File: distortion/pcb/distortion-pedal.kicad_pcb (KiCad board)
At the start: 4 copper layers, 29 x 45.2 mm, 73 parts, among them J1 AudioJack2_Ground, J2 AudioJack2_Ground, J3 USB4125-GF-A-0190, J4 Barrel_Jack, SW1 SW_DPDT_x2, U1 LMR62014XMF-NOPB, U2 TL081H, U3 TL081H, U4 TL081H, U5 TLV767, U6 TL081H

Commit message: distortion rev 3
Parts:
- removed RD3: R, Resistor_SMD:R_0805_2012Metric_Pad1.20x1.40mm_HandSolder
- added R18: R, Resistor_SMD:R_0805_2012Metric_Pad1.20x1.40mm_HandSolder, F.Cu at (54.1, 62.3)
- added R9: R, Resistor_SMD:R_0805_2012Metric_Pad1.20x1.40mm_HandSolder, F.Cu at (51.8, 66.7)
- added RF2: R, Resistor_SMD:R_0805_2012Metric_Pad1.20x1.40mm_HandSolder, F.Cu at (49.5, 65.1)
- D6: footprint Connector_PinHeader_2.54mm:PinHeader_1x02_P2.54mm_Vertical -> effect_pedal:led_wired_1_pin
- Gain1, Level1: footprint Connector_PinHeader_2.54mm:PinHeader_1x03_P2.54mm_Vertical -> effect_pedal:potentiometer_wired_23_connected
- J1, J2: footprint Connector_PinHeader_2.54mm:PinHeader_1x02_P2.54mm_Vertical -> effect_pedal:audio_jack_wired
- J4: footprint Connector_PinHeader_2.54mm:PinHeader_1x02_P2.54mm_Vertical -> effect_pedal:barrel_jack_wired
- L1: footprint Inductor_SMD:L_Abracon_ASPI-3012S -> Inductor_SMD:L_0805_2012Metric_Pad1.15x1.40mm_HandSolder
- SW1: footprint Connector_PinHeader_2.54mm:PinHeader_2x03_P2.54mm_Vertical -> effect_pedal:switch_wired
- Tone1: footprint Connector_PinHeader_2.54mm:PinHeader_1x03_P2.54mm_Vertical -> effect_pedal:potentiometer_wired_12_connected
- moved RF1 11.5 mm to (47.4, 65.1), turned to 90 degrees
- moved U3 9.32 mm to (67.4, 64.2)
- moved TP6 9.21 mm to (69.4, 67.4)
- moved R13 8.79 mm to (67.4, 68.5)
- moved D6 8.62 mm to (64.8, 69.4), turned to 180 degrees
- moved C8 8.11 mm to (69.8, 70.4)
- moved R4 8.08 mm to (71.2, 64.5), turned to 90 degrees
- moved R14 8.07 mm to (59.6, 74.8), turned to 90 degrees
- moved J1 7.91 mm to (48.3, 75.2), turned to 0 degrees
- moved J2 7.90 mm to (72.5, 75.2), turned to 180 degrees
- moved C6 7.12 mm to (62.8, 64.8), turned to 180 degrees
- moved SW1 7.10 mm to (64.7, 73.7), turned to 0 degrees
- moved C10 6.79 mm to (71.2, 60.2), turned to 90 degrees
- moved H4 6.52 mm to (73.0, 71.4)
- moved H3 6.52 mm to (48.0, 71.4)
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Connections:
- JPF1 pad 1: effect_in -> Net-(JPF1-Pad1)
- RD1 pad 1: effect_in -> Net-(JPF1-Pad1)
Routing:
- net +8V: track 10.0 -> 28.7 mm
- net +5V: track 14.9 -> 30.7 mm
- net +9V: track 0.00 -> 13.8 mm
- net Net-(D2-Pad2): track 0.00 -> 11.7 mm
- net Net-(C5-Pad2): track 0.00 -> 10.1 mm
- net Net-(JPF1-Pad1): track 0.00 -> 10.00 mm
- net Net-(C8-Pad1): track 0.00 -> 8.07 mm
- net Net-(Level1-Pad1): track 0.00 -> 7.24 mm
- net +4V: track 5.40 -> 12.6 mm
- net effect_in: track 4.24 -> 11.0 mm
- net Net-(C5-Pad1): track 0.00 -> 6.57 mm
- net Net-(D5-Pad2): track 0.00 -> 6.33 mm
- net Net-(C12-Pad2): track 0.00 -> 5.70 mm
- net Net-(R6-Pad2): track 4.43 -> 10.0 mm
- net Net-(D1-Pad1): track 26.7 -> 32.0 mm
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- removed copper zone on F.Cu, net +4V
- removed copper zone on F.Cu, net +5V
- removed copper zone on F.Cu, net +8V
- removed copper zone on F.Cu, net +9V
- removed copper zone on F.Cu, net Net-(C10-Pad1)
- removed copper zone on F.Cu, net Net-(C12-Pad2)
- removed copper zone on F.Cu, net Net-(C5-Pad1)
- removed copper zone on F.Cu, net Net-(C5-Pad2)
- removed copper zone on F.Cu, net Net-(C8-Pad1)
- removed copper zone on F.Cu, net Net-(D1-Pad1)
- removed copper zone on F.Cu, net Net-(D1-Pad2)
- removed copper zone on F.Cu, net Net-(D2-Pad2)
- removed copper zone on F.Cu, net Net-(D3-Pad2)
- removed copper zone on F.Cu, net Net-(D5-Pad2)
- removed copper zone on F.Cu, net Net-(D6-Pad2)
- removed copper zone on F.Cu, net Net-(Gain1-Pad2)
- removed copper zone on F.Cu, net Net-(J2-Pad2)
- removed copper zone on F.Cu, net Net-(JP2-Pad1)
- removed copper zone on F.Cu, net Net-(JPF1-Pad2)
- removed copper zone on F.Cu, net Net-(Level1-Pad1)
- removed copper zone on F.Cu, net Net-(R4-Pad1)
- removed copper zone on F.Cu, net Net-(R6-Pad1)
- removed copper zone on F.Cu, net Net-(R6-Pad2)
- removed copper zone on F.Cu, net audio_in
- removed copper zone on F.Cu, net effect_in
- removed copper zone on F.Cu, net effect_out
- removed copper zone on F.Cu, net gain_out
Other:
- board size 29 x 45.2 mm -> 30 x 37 mm
- board text added: "Fuzz/Distortion Pedal REV3"
- board text removed: "Fuzz/Distortion Pedal REV2"

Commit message: fix project error
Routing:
- net GND: vias 20 -> 24
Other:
- board text removed: "Active"

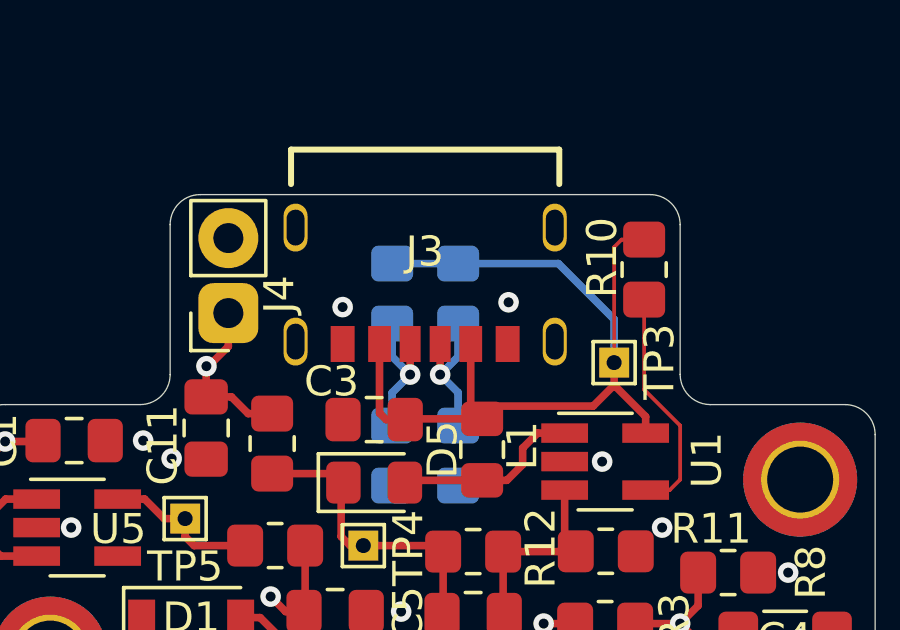
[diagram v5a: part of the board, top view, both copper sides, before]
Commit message: minor circuit rework for better use with multiple projects
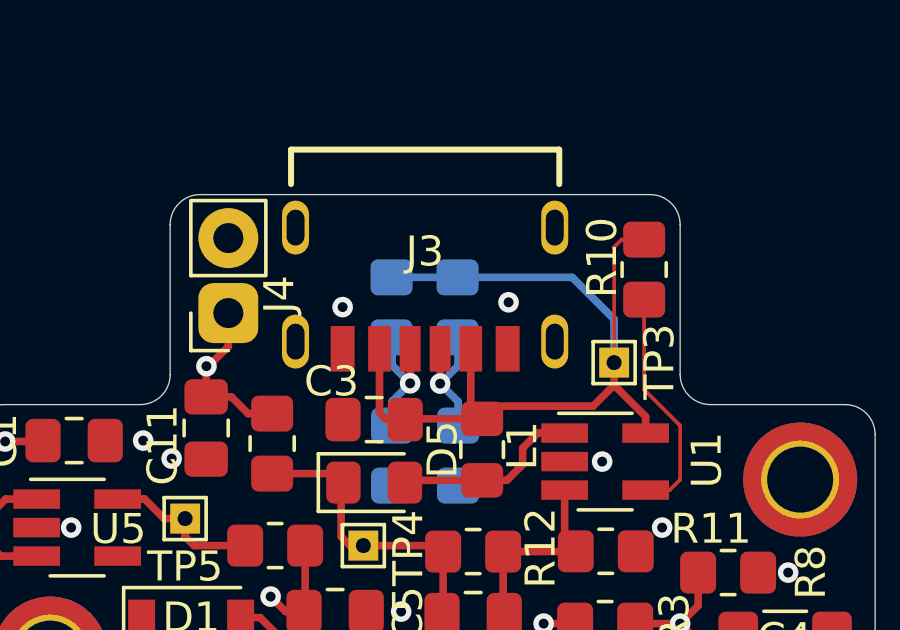
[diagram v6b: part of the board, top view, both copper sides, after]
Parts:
- moved Rcc3 0.46 mm to (61.6, 43.8)
- moved Rcc4 0.46 mm to (59.4, 43.8)
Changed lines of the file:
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@@
     (thickness 1.595)
   )
-  (paper "A4")
+  (paper "A5")
+  (title_block
+    (title "Distortion Pedal")
+  )
   (layers
     (0 "F.Cu" signal "Front")
@@
       (effects (font (size 1 1) (thickness 0.15)))
     )
-    (fp_line (start -4.47 2.25) (end -4.47 3.4) (layer "F.SilkS") (width 0.2))
     (fp_line (start -4.47 3.4) (end 4.47 3.4) (layer "F.SilkS") (width 0.2))
     (fp_line (start 4.47 3.4) (end 4.47 2.25) (layer "F.SilkS") (width 0.2))
-    (fp_line (start 5.15 3.65) (end -5.15 3.65) (layer "F.CrtYd") (width 0.05))
+    (fp_line (start -4.47 2.25) (end -4.47 3.4) (layer "F.SilkS") (width 0.2))
     (fp_line (start -5.15 -4.35) (end 5.15 -4.35) (layer "F.CrtYd") (width 0.05))
     (fp_line (start -5.15 3.65) (end -5.15 -4.35) (layer "F.CrtYd") (width 0.05))
     (fp_line (start 5.15 -4.35) (end 5.15 3.65) (layer "F.CrtYd") (width 0.05))
+    (fp_line (start 5.15 3.65) (end -5.15 3.65) (layer "F.CrtYd") (width 0.05))
+    (fp_line (start -4.47 3.4) (end -4.47 -3.4) (layer "F.Fab") (width 0.1))
     (fp_line (start 4.47 3.4) (end -4.47 3.4) (layer "F.Fab") (width 0.1))
-    (fp_line (start -4.47 3.4) (end -4.47 -3.4) (layer "F.Fab") (width 0.1))
+    (fp_line (start 4.47 -3.4) (end 4.47 3.4) (layer "F.Fab") (width 0.1))
     (fp_line (start -4.47 -3.4) (end 4.47 -3.4) (layer "F.Fab") (width 0.1))
-    (fp_line (start 4.47 -3.4) (end 4.47 3.4) (layer "F.Fab") (width 0.1))
-    (pad "A5" smd rect (at -0.5 -3.08 180) (size 0.7 1.2) (layers "F.Cu" "F.Paste" "F.Mask")
+    (pad "A5" smd rect (at -0.5 -3.24 180) (size 0.7 1.52) (layers "F.Cu" "F.Paste" "F.Mask")
       (net 16 "Net-(J3-PadA5)") (pinfunction "CC1") (pintype "bidirectional"))
-    (pad "A9" smd rect (at 1.52 -3.08 180) (size 0.76 1.2) (layers "F.Cu" "F.Paste" "F.Mask")
+    (pad "A9" smd rect (at 1.52 -3.24 180) (size 0.76 1.52) (layers "F.Cu" "F.Paste" "F.Mask")
       (net 10 "+5V") (pinfunction "VBUS") (pintype "power_in"))
-    (pad "A12" smd rect (at 2.75 -3.08 180) (size 0.8 1.2) (layers "F.Cu" "F.Paste" "F.Mask")
+    (pad "A12" smd rect (at 2.75 -3.24 180) (size 0.8 1.52) (layers "F.Cu" "F.Paste" "F.Mask")
       (net 1 "GND") (pinfunction "GND") (pintype "power_in"))
-    (pad "B5" smd rect (at 0.5 -3.08 180) (size 0.7 1.2) (layers "F.Cu" "F.Paste" "F.Mask")
+    (pad "B5" smd rect (at 0.5 -3.24 180) (size 0.7 1.52) (layers "F.Cu" "F.Paste" "F.Mask")
       (net 17 "Net-(J3-PadB5)") (pinfunction "CC2") (pintype "bidirectional"))
-    (pad "B9" smd rect (at -1.52 -3.08 180) (size 0.76 1.2) (layers "F.Cu" "F.Paste" "F.Mask")
+    (pad "B9" smd rect (at -1.52 -3.24 180) (size 0.76 1.52) (layers "F.Cu" "F.Paste" "F.Mask")
       (net 10 "+5V") (pinfunction "VBUS") (pintype "power_in"))
-    (pad "B12" smd rect (at -2.75 -3.08 180) (size 0.8 1.2) (layers "F.Cu" "F.Paste" "F.Mask")
+    (pad "B12" smd rect (at -2.75 -3.24 180) (size 0.8 1.52) (layers "F.Cu" "F.Paste" "F.Mask")
       (net 1 "GND") (pinfunction "GND") (pintype "power_in"))
-    (pad "S1" thru_hole oval (at -4.32 -3 180) (size 0.8 1.6) (drill oval 0.6 1.2) (layers *.Cu)
+    (pad "S1" thru_hole oval (at -4.32 -3 180) (size 0.9 1.8) (drill oval 0.6 1.2) (layers *.Cu *.Mask)
       (net 1 "GND") (pinfunction "SHIELD") (pintype "passive"))
-    (pad "S2" thru_hole oval (at 4.32 -3 180) (size 0.8 1.6) (drill oval 0.6 1.2) (layers *.Cu)
+    (pad "S2" thru_hole oval (at 4.32 -3 180) (size 0.9 1.8) (drill oval 0.6 1.2) (layers *.Cu *.Mask)
       (net 1 "GND") (pinfunction "SHIELD") (pintype "passive"))
-    (pad "S3" thru_hole oval (at -4.32 0.8 180) (size 0.8 1.6) (drill oval 0.6 1.2) (layers *.Cu)
+    (pad "S3" thru_hole oval (at -4.32 0.8 180) (size 0.9 1.8) (drill oval 0.6 1.2) (layers *.Cu *.Mask)
       (net 1 "GND") (pinfunction "SHIELD") (pintype "passive"))
-    (pad "S4" thru_hole oval (at 4.32 0.8 180) (size 0.8 1.6) (drill oval 0.6 1.2) (layers *.Cu)
+    (pad "S4" thru_hole oval (at 4.32 0.8 180) (size 0.9 1.8) (drill oval 0.6 1.2) (layers *.Cu *.Mask)
       (net 1 "GND") (pinfunction "SHIELD") (pintype "passive"))
     (model "/Users/lukas/Documents/KiCad/6.0/3dmodels/USB4125-GF-A-0190_REVA2.step"
@@
   )
   (footprint "Resistor_SMD:R_0805_2012Metric_Pad1.20x1.40mm_HandSolder" (layer "B.Cu")
-    (at 61.6 43.3 -90)
+    (at 61.58 43.76 -90)
     (descr "Resistor SMD 0805 (2012 Metric), square (rectangular) end terminal, IPC_7351 nominal with elongated pad for handsoldering. (Body size source: IPC-SM-782 page 72, https://www.pcb-3d.com/wordpress/wp-content/uploads/ipc-sm-782a_amendment_1_and_2.pdf), generated with kicad-footprint-generator")
     (tags "resistor handsolder")
@@
   )
   (footprint "Resistor_SMD:R_0805_2012Metric_Pad1.20x1.40mm_HandSolder" (layer "B.Cu")
-    (at 59.4 43.3 -90)
+    (at 59.38 43.76 -90)
     (descr "Resistor SMD 0805 (2012 Metric), square (rectangular) end terminal, IPC_7351 nominal with elongated pad for handsoldering. (Body size source: IPC-SM-782 page 72, https://www.pcb-3d.com/wordpress/wp-content/uploads/ipc-sm-782a_amendment_1_and_2.pdf), generated with kicad-footprint-generator")
     (tags "resistor handsolder")
@@
   (segment (start 62.02 47.12) (end 62.02 44.98) (width 0.254) (layer "F.Cu") (net 10))
   (segment (start 58.98 44.98) (end 58.98 47.28) (width 0.254) (layer "F.Cu") (net 10))
+  (segment (start 66.8 44.16) (end 65.4 42.76) (width 0.254) (layer "B.Cu") (net 10))
+  (segment (start 61.58 42.76) (end 59.38 42.76) (width 0.254) (layer "B.Cu") (net 10))
+  (segment (start 65.4 42.76) (end 61.58 42.76) (width 0.254) (layer "B.Cu") (net 10))
   (segment (start 66.8 44.16) (end 66.8 45.6) (width 0.254) (layer "B.Cu") (net 10))
-  (segment (start 64.94 42.3) (end 66.8 44.16) (width 0.254) (layer "B.Cu") (net 10))
-  (segment (start 61.6 42.3) (end 64.94 42.3) (width 0.254) (layer "B.Cu") (net 10))
-  (segment (start 59.4 42.3) (end 61.6 42.3) (width 0.254) (layer "B.Cu") (net 10))
   (segment (start 57.475 49.3) (end 57.775 49.6) (width 0.254) (layer "F.Cu") (net 11))
   (segment (start 57.775 49.6) (end 57.7 49.675) (width 0.254) (layer "F.Cu") (net 11))
@@
   (segment (start 71.55 57.25) (end 71.55 57.55) (width 0.254) (layer "F.Cu") (net 15))
   (segment (start 71.55 57.55) (end 73.9 57.55) (width 0.254) (layer "F.Cu") (net 15))
-  (segment (start 61 44.98) (end 61 46) (width 0.254) (layer "F.Cu") (net 16))
-  (via (at 61 46) (size 0.6858) (drill 0.3302) (layers "F.Cu" "B.Cu") (net 16))
-  (segment (start 61.6 44.3) (end 61.6 45.4) (width 0.254) (layer "B.Cu") (net 16))
-  (segment (start 61.6 45.4) (end 61 46) (width 0.254) (layer "B.Cu") (net 16))
-  (segment (start 61.6 46.6) (end 61.6 47.7) (width 0.254) (layer "B.Cu") (net 16))
-  (segment (start 61 46) (end 61.6 46.6) (width 0.254) (layer "B.Cu") (net 16))
-  (segment (start 60 44.98) (end 60 46) (width 0.254) (layer "F.Cu") (net 17))
-  (via (at 60 46) (size 0.6858) (drill 0.3302) (layers "F.Cu" "B.Cu") (net 17))
-  (segment (start 59.4 44.3) (end 59.4 45.4) (width 0.254) (layer "B.Cu") (net 17))
-  (segment (start 59.4 45.4) (end 60 46) (width 0.254) (layer "B.Cu") (net 17))
-  (segment (start 59.4 46.6) (end 59.4 47.7) (width 0.254) (layer "B.Cu") (net 17))
-  (segment (start 60 46) (end 59.4 46.6) (width 0.254) (layer "B.Cu") (net 17))
+  (segment (start 61 44.98) (end 61 46.3) (width 0.254) (layer "F.Cu") (net 16))
+  (via (at 61 46.3) (size 0.6858) (drill 0.3302) (layers "F.Cu" "B.Cu") (net 16))
+  (segment (start 61.6 46.9) (end 61.6 47.7) (width 0.254) (layer "B.Cu") (net 16))
+  (segment (start 61.6 45.7) (end 61.6 44.3) (width 0.254) (layer "B.Cu") (net 16))
+  (segment (start 61 46.3) (end 61.6 45.7) (width 0.254) (layer "B.Cu") (net 16))
+  (segment (start 61 46.3) (end 61.6 46.9) (width 0.254) (layer "B.Cu") (net 16))
+  (segment (start 60 44.98) (end 60 46.29) (width 0.254) (layer "F.Cu") (net 17))
+  (via (at 60 46.29) (size 0.6858) (drill 0.3302) (layers "F.Cu" "B.Cu") (net 17))
+  (segment (start 59.4 46.89) (end 59.4 47.7) (width 0.254) (layer "B.Cu") (net 17))
+  (segment (start 60 46.29) (end 59.4 46.89) (width 0.254) (layer "B.Cu") (net 17))
+  (segment (start 60 46.29) (end 59.4 45.69) (width 0.254) (layer "B.Cu") (net 17))
+  (segment (start 59.4 45.69) (end 59.4 44.3) (width 0.254) (layer "B.Cu") (net 17))
   (segment (start 67.3 69.4) (end 67.4 69.5) (width 0.254) (layer "F.Cu") (net 18))
   (segment (start 64.85 69.4) (end 67.3 69.4) (width 0.254) (layer "F.Cu") (net 18))
